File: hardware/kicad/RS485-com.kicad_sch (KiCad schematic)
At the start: 11 parts, among them J4 Conn_01x02_Socket, SW2 SW_DIP_x01, SW3 VCC485BiasSW, SW4 SW_DIP_x01

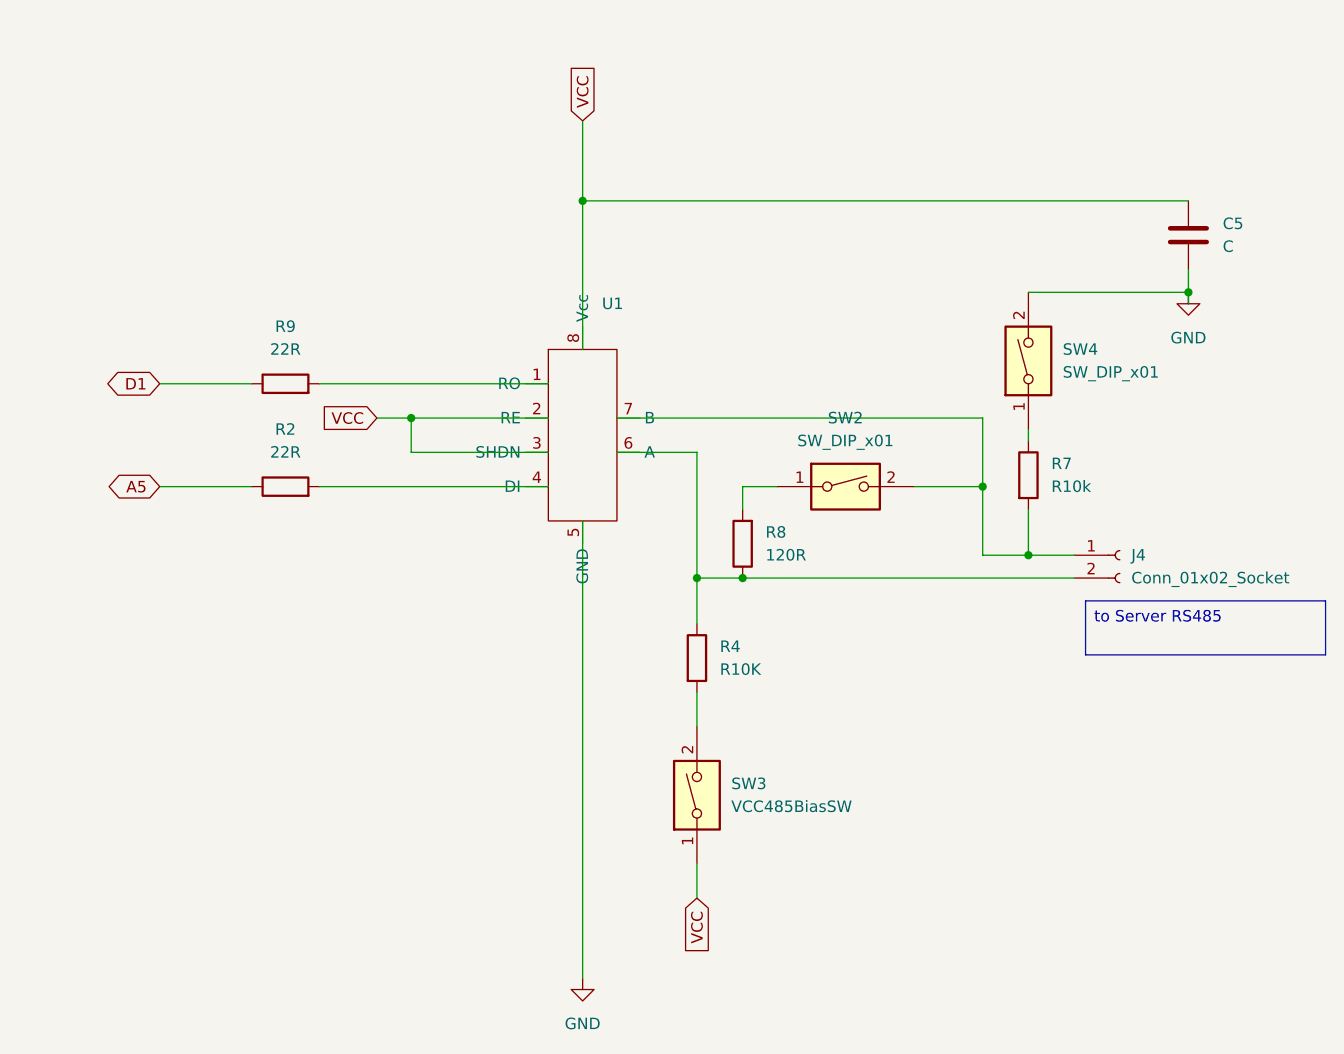
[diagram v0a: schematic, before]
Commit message: chore: KiCad 회로도 최신 변경사항 반영
원본 작업 폴더가 "회로도 편집 완료/20260901_ver01"로 재구성됨(이전 smartvault-pcb-1
경로는 더 이상 존재하지 않음). 하위 시트 6개 전부와 최상위 시트에 실제 설계 변경
있음(DoorRock-drv는 축소, 최상위 시트는 대폭 확장 — 회로가 재구성된 것으로 보임).
PCB 레이아웃 자체는 변경 없음. footprint.xlsx(부품-풋프린트 매핑) 신규 추가.

파일 내부의 프로젝트명 자기참조는 원본 작업 파일명("20260901_ver01")이 아니라
저장소 표준 이름("smartvault")으로 맞춰서 복사 — 작업 폴더 쪽 날짜/버전 파일명
관례를 저장소까지 끌고 오지 않음(git이 버전을 관리).

s_vault.kicad_sym(커스텀 심볼 라이브러리)은 원본 경로에서 찾지 못해 갱신 못함 —
RS485-com/power 시트가 이 라이브러리를 참조하므로, 최신 심볼이 바뀌었다면 다음에
갱신 필요(hardware/README.md에 기록해둠).

Co-Authored-By: Claude Sonnet 5 <noreply@anthropic.com>
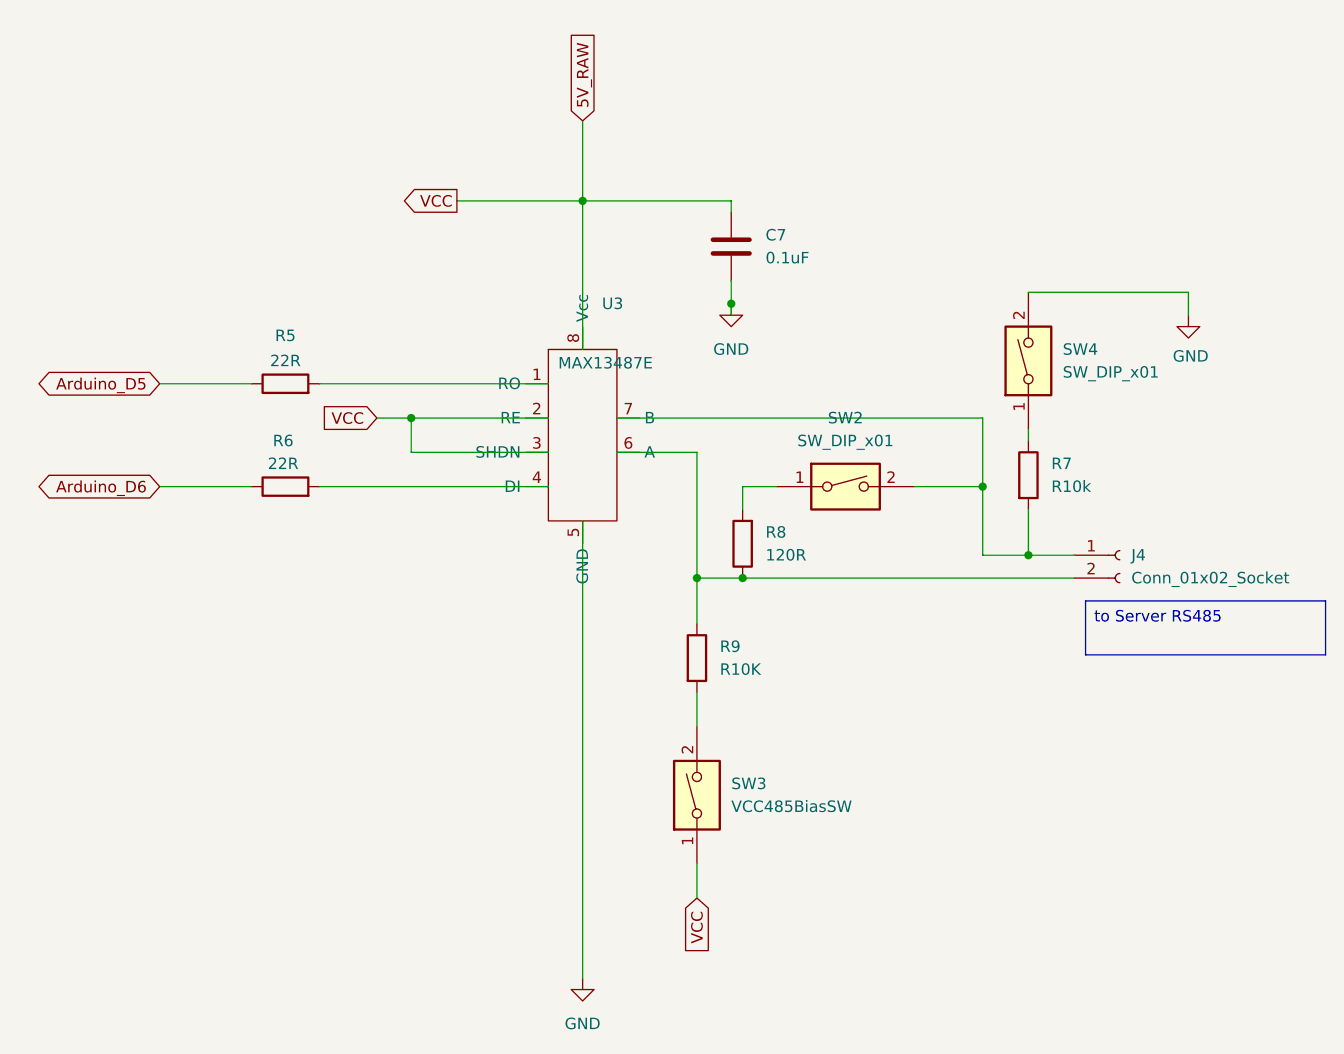
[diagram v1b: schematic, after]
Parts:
- removed C5: C, symbol Device:C
- added C7: 0.1uF, Capacitor_SMD:C_0805_2012Metric, symbol Device:C
- J4: footprint (none) -> Connector_JST:JST_XH_B2B-XH-A_1x02_P2.50mm_Vertical
- R5: renamed from R9; footprint (none) -> Resistor_SMD:R_0805_2012Metric
- R6: renamed from R2; footprint (none) -> Resistor_SMD:R_0805_2012Metric
- R7, R8: footprint (none) -> Resistor_SMD:R_0805_2012Metric
- R9: renamed from R4; footprint (none) -> Resistor_SMD:R_0805_2012Metric
- SW2: footprint (none) -> Button_Switch_THT:SW_DIP_SPSTx01_Slide_9.78x4.72mm_W7.62mm_P2.54mm
- renumbered U1 to U3
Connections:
- net GND: now also C7.2
- net A5 renamed Arduino_D6
- net D1 renamed Arduino_D5
- net VCC renamed 5V_RAW
- net 5V_RAW: now also C7.1
